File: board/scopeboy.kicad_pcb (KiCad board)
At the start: 4 copper layers, 100 x 80 mm, 135 parts, among them J1 USB_C_Receptacle_USB2.0_16P, J2 SM03B-SRSS-TB, J3 SM03B-SRSS-TB, J4 Conn_01x10, J5 SM04B-SRSS-TB, J6 HDMI_A, J7 731000105, SW1 SW_Push, SW2 SW_Push, SW3 RotaryEncoder_Switch, U1 W25Q128JVS, U10 LMH6629, U11 OPA820, U12 DAC5571, U13 LM4040DBZ-2.0, U14 TLV3501, U15 DAC5571, U16 TLV9101, U2 DNF, U3 NCP1117-3.3_SOT223, U4 RP2350_80QFN, U5 LP2985-3.3, U6 LM27762, U7 ADC08060, U8 OPA354, U9 ADG621, Y1 ABM8-272-T3

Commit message: Updated trig, sel0, sel1 pins
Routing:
- removed copper zone on In1.Cu, net GND
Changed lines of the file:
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@@
 		(min_thickness 0.25)
 		(filled_areas_thickness no)
-		(fill
+		(fill yes
 			(thermal_gap 0.508)
 			(thermal_bridge_width 0.508)
@@
 		(min_thickness 0.2)
 		(filled_areas_thickness no)
-		(fill
+		(fill yes
 			(thermal_gap 0.3)
 			(thermal_bridge_width 0.3)
@@
 		(min_thickness 0.2)
 		(filled_areas_thickness no)
-		(fill
+		(fill yes
 			(thermal_gap 0.3)
 			(thermal_bridge_width 0.3)
@@
 		(min_thickness 0.254)
 		(filled_areas_thickness no)
-		(fill
+		(fill yes
 			(thermal_gap 0.508)
 			(thermal_bridge_width 0.508)
@@
 		(min_thickness 0.15)
 		(filled_areas_thickness no)
-		(fill
+		(fill yes
 			(thermal_gap 0.5)
 			(thermal_bridge_width 0.5)
@@
 		(min_thickness 0.15)
 		(filled_areas_thickness no)
-		(fill
+		(fill yes
 			(thermal_gap 0.5)
 			(thermal_bridge_width 0.5)
@@
 		(min_thickness 0.15)
 		(filled_areas_thickness no)
-		(fill
+		(fill yes
 			(thermal_gap 0.5)
 			(thermal_bridge_width 0.5)
@@
 		(min_thickness 0.15)
 		(filled_areas_thickness no)
-		(fill
+		(fill yes
 			(thermal_gap 0.5)
 			(thermal_bridge_width 0.5)
@@
 		(min_thickness 0.254)
 		(filled_areas_thickness no)
-		(fill
+		(fill yes
 			(thermal_gap 0.508)
 			(thermal_bridge_width 0.508)
@@
 		(min_thickness 0.254)
 		(filled_areas_thickness no)
-		(fill
+		(fill yes
 			(thermal_gap 0.508)
 			(thermal_bridge_width 0.508)
@@
 		(min_thickness 0.254)
 		(filled_areas_thickness no)
-		(fill
+		(fill yes
 			(thermal_gap 0.508)
 			(thermal_bridge_width 0.508)
@@
 				(xy 221.15 150.545) (xy 165.65 150.545) (xy 165.65 113.545) (xy 169.65 113.545) (xy 169.65 104.545)
 				(xy 165.65 104.545) (xy 165.65 69.045) (xy 221.15 69.045)
-			)
-		)
-	)
-	(zone
-		(net 1)
-		(net_name "GND")
-		(layer "In1.Cu")
-		(hatch edge 0.508)
-		(connect_pads
-			(clearance 0.508)
-		)
-		(min_thickness 0.254)
-		(filled_areas_thickness no)
-		(fill
-			(thermal_gap 0.508)
-			(thermal_bridge_width 0.508)
-		)
-		(polygon
-			(pts
-				(xy 221.65 150.545) (xy 165.65 150.545) (xy 165.65 113.545) (xy 169.65 113.545) (xy 169.65 104.545)
-				(xy 165.65 104.545) (xy 165.65 69.545) (xy 221.65 69.545)
 			)
 		)
@@
 		(min_thickness 0.254)
 		(filled_areas_thickness no)
-		(fill
-			(thermal_gap 0.508)
-			(thermal_bridge_width 0.508)
-		)
-		(polygon
-			(pts
-				(xy 165.65 104.545) (xy 169.65 104.545) (xy 169.65 113.545) (xy 165.65 113.545) (xy 165.65 150.545)
-				(xy 120.65 150.545) (xy 120.65 133.545) (xy 120.65 69.545) (xy 165.65 69.545)
+		(fill yes
+			(thermal_gap 0.508)
+			(thermal_bridge_width 0.508)
+		)
+		(polygon
+			(pts
+				(xy 220.65 104.545) (xy 220.65 104.545) (xy 220.65 113.545) (xy 220.65 113.545) (xy 220.65 150.545)
+				(xy 120.65 150.545) (xy 120.65 133.545) (xy 120.65 69.545) (xy 220.65 69.545)
 			)
 		)
@@
 		(min_thickness 0.25)
 		(filled_areas_thickness no)
-		(fill
+		(fill yes
 			(thermal_gap 0.5)
 			(thermal_bridge_width 0.5)
@@
 		(min_thickness 0.254)
 		(filled_areas_thickness no)
-		(fill
+		(fill yes
 			(thermal_gap 0.508)
 			(thermal_bridge_width 0.508)
@@
 		(min_thickness 0.254)
 		(filled_areas_thickness no)
-		(fill
+		(fill yes
 			(thermal_gap 0.508)
 			(thermal_bridge_width 0.508)
@@
 		(min_thickness 0.254)
 		(filled_areas_thickness no)
-		(fill
-			(thermal_gap 0.508)
-			(thermal_bridge_width 0.508)
+		(fill yes
+			(thermal_gap 0.508)
+			(thermal_bridge_width 0.508)

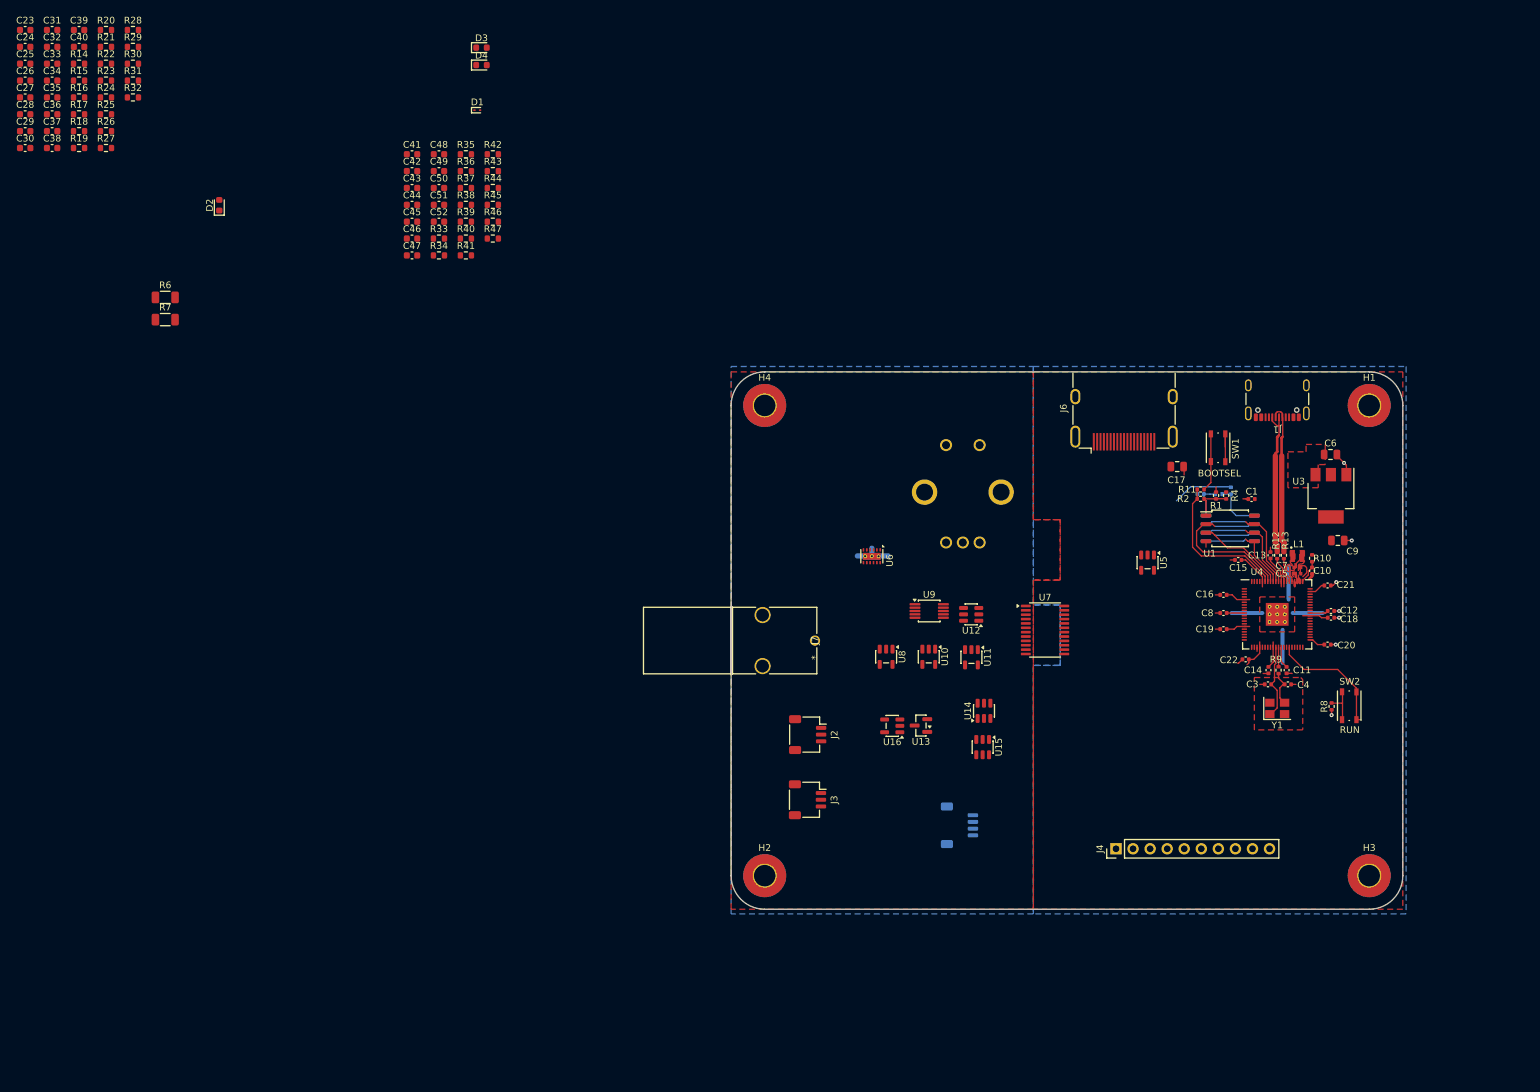
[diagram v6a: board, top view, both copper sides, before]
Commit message: Added battery JST connector
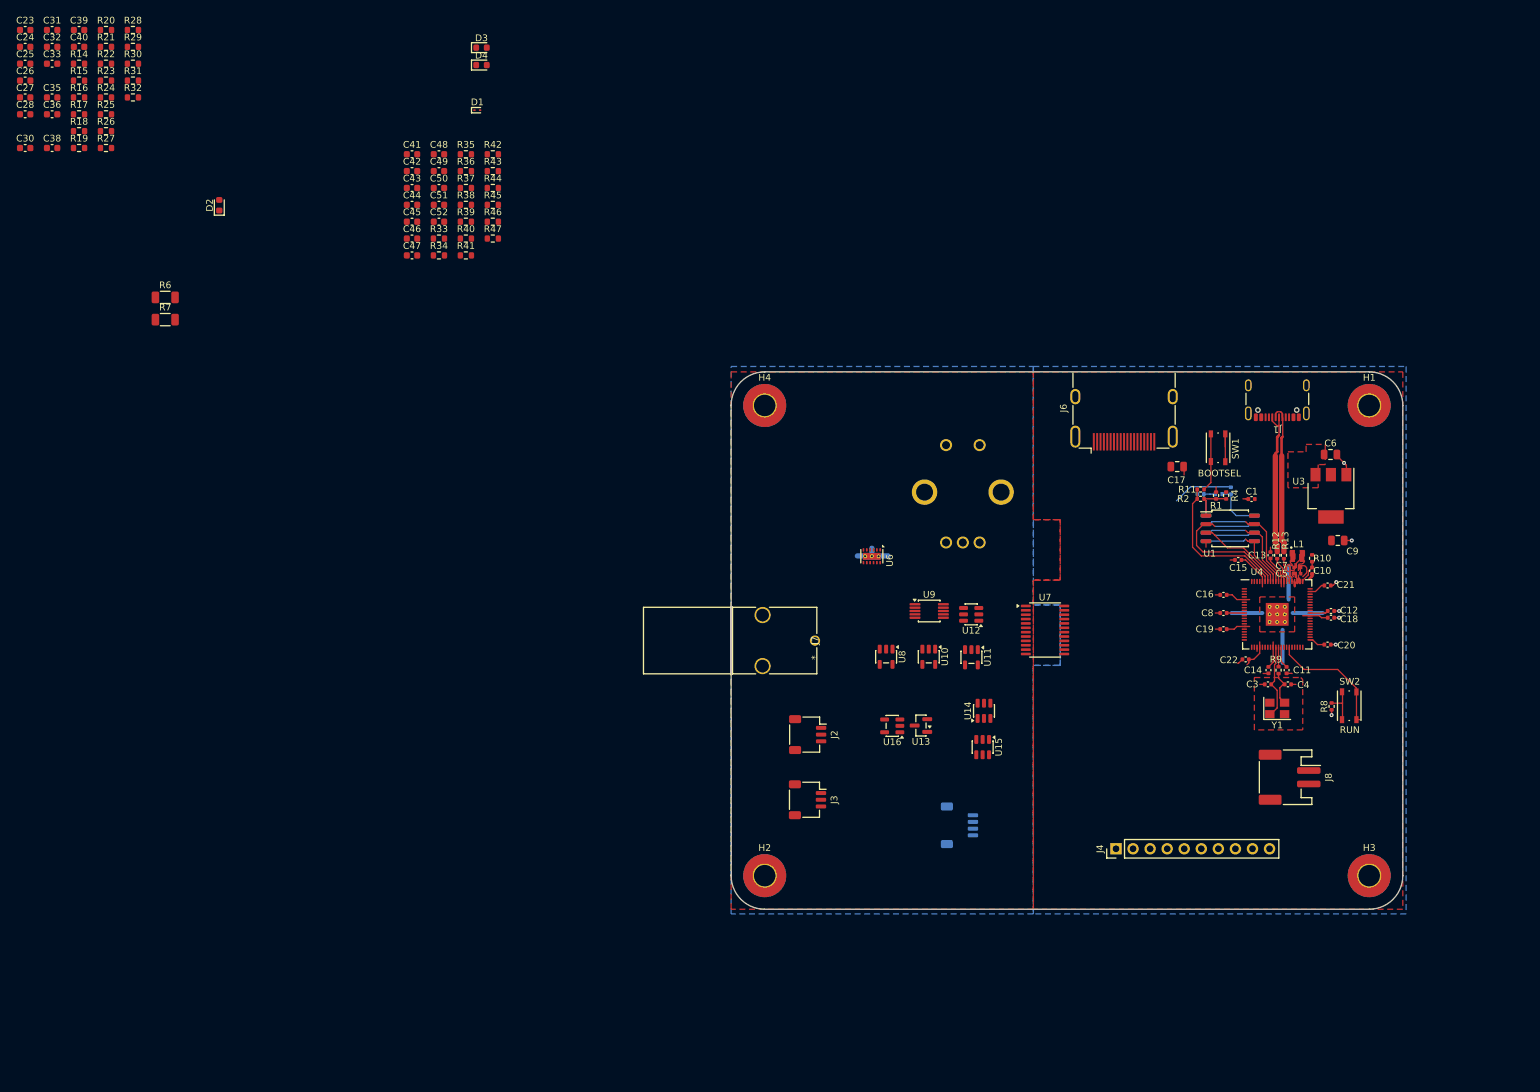
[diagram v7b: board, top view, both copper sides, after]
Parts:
- removed C29: 1u, Capacitor_SMD:C_0603_1608Metric
- removed C34: 10n, Capacitor_SMD:C_0603_1608Metric
- removed C37: 2.2u, Capacitor_SMD:C_0603_1608Metric
- removed U5: LP2985-3.3, Package_TO_SOT_SMD:SOT-23-5
- added J8: Conn_01x02, Connector_JST:JST_PH_S2B-PH-SM4-TB_1x02-1MP_P2.00mm_Horizontal, F.Cu at (203.8, 130.2)
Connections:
- C26 pad 1: VSYS -> VBUS
- D1 pad 2: /Analog Front End/CHASSIS -> GNDA
- J7 pad 2: /Analog Front End/CHASSIS -> GNDA
- U4 pad 1: /GPIO4 -> /TRIG
- U4 pad 2: /GPIO5 -> /Sel0
- U4 pad 3: /GPIO6 -> /Sel1
- U6 pad 12: VSYS -> VBUS
- U6 pad 3: VSYS -> VBUS
- U6 pad 8: VSYS -> VBUS
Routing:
- added copper zone on In2.Cu, net VBUS
- removed copper zone on In2.Cu, net VSYS

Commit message: Added power mux and USB protection
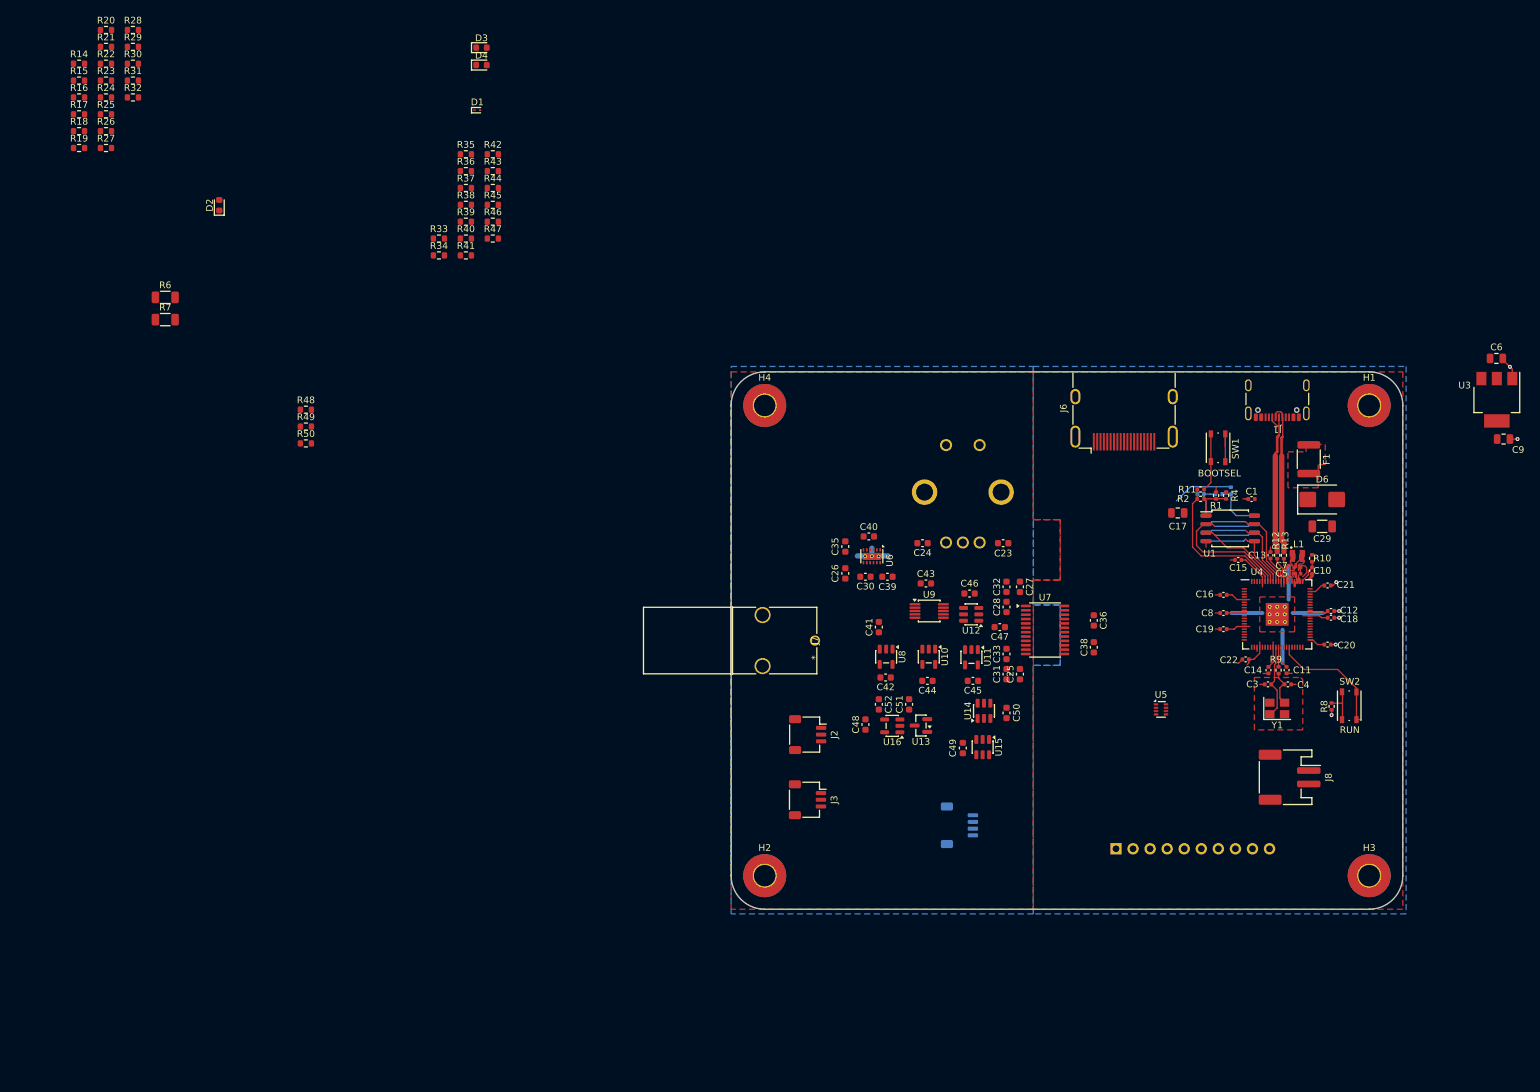
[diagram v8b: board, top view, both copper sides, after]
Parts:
- added C29: 10uF, Capacitor_SMD:C_1206_3216Metric, F.Cu at (208.7, 92.8)
- added D6: SMBJ5.0A, Diode_SMD:D_SMB, F.Cu at (208.7, 88.8)
- added F1: MINISMDC050F-2, Fuse:Fuse_1812_4532Metric, F.Cu at (206.7, 82.8)
- added R48: 100k, Resistor_SMD:R_0603_1608Metric, F.Cu at (57.3, 75.5)
- added R49: 10K, Resistor_SMD:R_0603_1608Metric, F.Cu at (57.3, 78.0)
- added R50: 47k, Resistor_SMD:R_0603_1608Metric, F.Cu at (57.3, 80.5)
- added U5: TPS2116DRL, Package_TO_SOT_SMD:SOT-583-8, F.Cu at (184.7, 120.1)
- J4: moved to B.Cu
- moved C25 173.8 mm to (163.7, 114.8), turned to 90 degrees
- moved C36 172.4 mm to (174.7, 106.8), turned to -90 degrees
- moved C38 172.0 mm to (174.7, 110.8), turned to 90 degrees
- moved C31 171.4 mm to (161.7, 114.8), turned to 90 degrees
- moved C33 167.1 mm to (161.7, 111.8), turned to 90 degrees
- moved C27 165.0 mm to (163.7, 101.8), turned to -90 degrees
- moved C23 164.4 mm to (161.2, 95.3)
- moved C28 163.5 mm to (161.7, 104.8), turned to 90 degrees
- moved C32 163.3 mm to (161.7, 101.8), turned to 90 degrees
- moved C24 152.7 mm to (149.2, 95.3), turned to 180 degrees
- moved C39 145.3 mm to (143.9, 100.3)
- moved C26 142.4 mm to (137.7, 99.8), turned to -90 degrees
- moved C30 140.4 mm to (140.7, 100.3), turned to 180 degrees
- moved C40 138.3 mm to (141.2, 94.3)
- moved C35 135.7 mm to (137.7, 95.8), turned to -90 degrees
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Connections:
- net /GPIO16 renamed /HDMI_D1P
- net /GPIO17 renamed /HDMI_D1N
- net /GPIO18 renamed /HDMI_D0P
- net /GPIO19 renamed /HDMI_D0N
- C6 pad 1: VBUS -> VDC
- J1 pad A4: VBUS -> Net-(F1-Pad1)
- J1 pad A9: VBUS -> Net-(F1-Pad1)
- J1 pad B4: VBUS -> Net-(F1-Pad1)
- J1 pad B9: VBUS -> Net-(F1-Pad1)
- J1 pad S1: unconnected-(J1-SHIELD-PadS1) -> GND
- J6 pad 18: +5V -> VBUS
- J8 pad 1: VBUS -> /VBat
- R19 pad 1: +5V -> VBUS
- R19 pad 2: +5V -> VBUS
- R24 pad 2: /GPIO12 -> /HDMI_D2P
- R25 pad 2: /GPIO13 -> /HDMI_D2N
- R30 pad 2: /GPIO14 -> /HDMI_CKP
- R31 pad 2: /GPIO15 -> /HDMI_CKN
- U3 pad 3: VBUS -> VDC
- U4 pad 11: /D4 -> /HDMI_D2P
- U4 pad 12: /D5 -> /HDMI_D2N
- U4 pad 13: /D6 -> /HDMI_CKP
- U4 pad 14: /D7 -> /HDMI_CKN
- U4 pad 4: /GPIO7 -> /PowerStatus
- U4 pad 40: /GPIO32 -> /D0
- U4 pad 42: /GPIO33 -> /D1
- U4 pad 43: /GPIO34 -> /D2
- U4 pad 44: /GPIO35 -> /D3
- U4 pad 45: /GPIO36 -> /D4
- U4 pad 46: /GPIO37 -> /D5
- U4 pad 47: /GPIO38 -> /D6
- U4 pad 48: /GPIO39 -> /D7
- U4 pad 6: /D0 -> unconnected-(U4-GPIO8-Pad6)
- U4 pad 7: /D1 -> unconnected-(U4-GPIO9-Pad7)
- U4 pad 8: /D2 -> unconnected-(U4-GPIO10-Pad8)
- U4 pad 9: /D3 -> unconnected-(U4-GPIO11-Pad9)
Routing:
- net GND: track 26.4 -> 25.2 mm
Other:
- board text added: "ScopeBoy Designed by Robbie Leslie, Immanuel Koshy Cornell University Department of Electrical and Computer Engineering"
